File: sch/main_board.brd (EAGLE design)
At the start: 70 x 50 mm, 17 parts, among them IC1 MCP73831T-2ACI_OT, J1 MICRO_USB_B_HIROSE_ZX62-B-5PA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

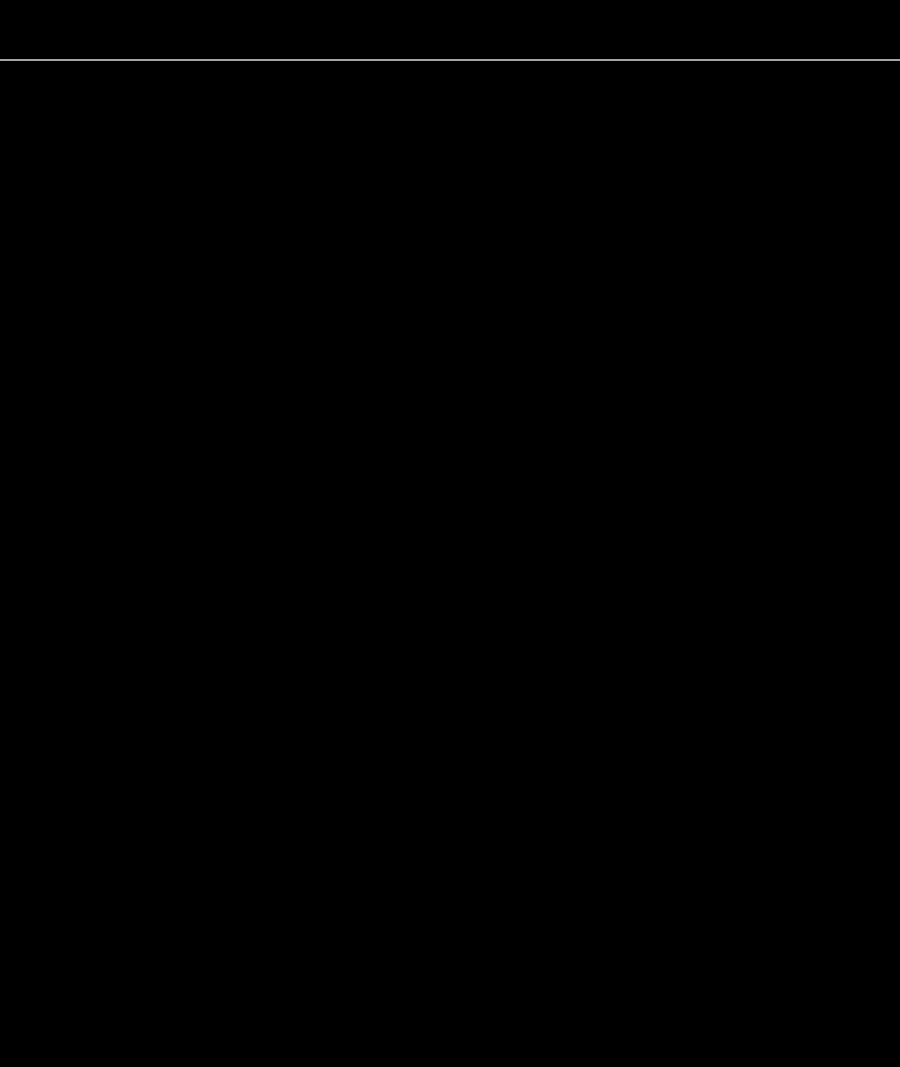
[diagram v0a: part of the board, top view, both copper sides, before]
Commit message: Add MPU design block
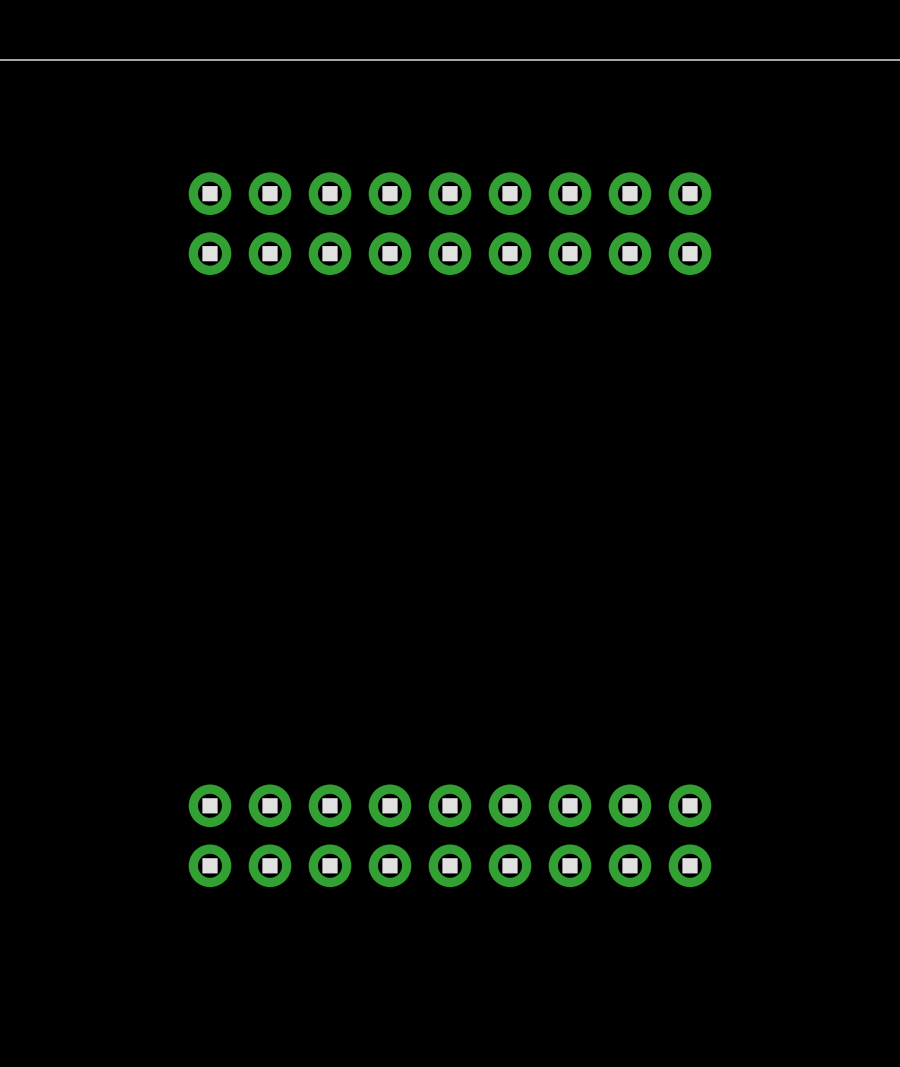
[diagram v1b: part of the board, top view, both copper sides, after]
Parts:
- added U$6, U$7: 2X9, headers(2mm):2X9
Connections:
- new net P0.00: U$6.14
- new net P0.01: U$6.15
- new net P0.02: U$6.16
- new net P0.03: U$6.17
- new net P0.04: U$6.18
- new net P0.05: U$7.17
- new net P0.06: U$7.18
- new net P0.07: U$7.15
- new net P0.08: U$7.16
- new net P0.09: U$7.13
- new net P0.10: U$7.14
- new net P0.11: U$7.11
- new net P0.12: U$7.12
- new net P0.13: U$7.9
- new net P0.14: U$7.10
- new net P0.15: U$7.7
- new net P0.16: U$7.8
- new net P0.17: U$7.3
- new net P0.18: U$7.1
- new net P0.19: U$7.4
- new net P0.20: U$7.2
- new net P0.21: U$6.2
- new net P0.22: U$6.3
- new net P0.23: U$6.4
- new net P0.24: U$6.5
- new net P0.25: U$6.6
- new net P0.28: U$6.9
- new net P0.29: U$6.10
- new net P0.30: U$6.13
- new net SWDCLK: U$7.6
- new net SWDIO: U$7.5
- new net VDD: U$6.11
- net GND: now also U$6.1, U$6.12
